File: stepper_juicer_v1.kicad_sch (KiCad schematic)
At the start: 12 parts, among them J1 Conn_01x06_Pin, J2 Barrel_Jack_Switch

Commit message: Schematic done
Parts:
- added C1, C11, C12, C14, C15, C6, C8, C9: 1uF 50V, Capacitor_SMD:C_0402_1005Metric, symbol Device:C
- added C10, C13, C3, C4, C7: 10uF 50V, Capacitor_SMD:C_0805_2012Metric, symbol Device:C
- added C2: 470uF 50V, Capacitor_THT:CP_Radial_D10.0mm_P5.00mm, symbol Device:C_Polarized_US
- added C5: 1uF 100V, Capacitor_SMD:C_0805_2012Metric, symbol Device:C
- added D1, D2, D3, D4: 30V 200mA, Diode_SMD:D_SOD-523, symbol Device:D_Schottky
- added D5, D6, D7, D8: 100V 2A, Diode_SMD:Nexperia_CFP3_SOD-123W, symbol Device:D_Schottky
- added D9: LED, Diode_SMD:D_0603_1608Metric, symbol Device:LED
- added J3: Conn_01x04_Pin, Connector_JST:JST_XH_B4B-XH-A_1x04_P2.50mm_Vertical, symbol Connector:Conn_01x04_Pin
- added J4: Conn_01x06_Pin, Connector_JST:JST_PH_B6B-PH-K_1x06_P2.00mm_Vertical, symbol Connector:Conn_01x06_Pin
- added Q1, Q2, Q3, Q4, Q5, Q6, Q7, Q8: NMOS, _custom_library: PG-TSDSON-8_3.8x2.29_Pitch0.65mm, symbol Simulation_SPICE:NMOS
- added R11, R13, R14, R16, R17, R19, R20: 4.7R, Resistor_SMD:R_0805_2012Metric, symbol Device:R_US
- added R12, R15, R18: 8.2R, Resistor_SMD:R_0805_2012Metric, symbol Device:R_US
- added R21: 8k2, Resistor_SMD:R_0603_1608Metric, symbol Device:R_US
- added U1, U2, U4, U5: NCP51513, Package_DFN_QFN:DFN-10-1EP_3x3mm_P0.5mm_EP1.7x2.5mm, symbol _custom_library:NCP51513
- added U3: ZXTR2012Z, Package_TO_SOT_SMD:SOT-89-3, symbol _custom_library:ZXTR2012Z
- J1: footprint (none) -> Connector_JST:JST_PH_B6B-PH-K_1x06_P2.00mm_Vertical; Link (none) -> https://www.digikey.ca/en/products/detail/jst-sales-america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
- J2: footprint (none) -> Connector_BarrelJack:BarrelJack_GCT_DCJ200-10-A_Horizontal; Link (none) -> https://www.digikey.ca/en/products/detail/tensility-interna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
- R1, R2: value 1k5 -> 2k0; footprint (none) -> Resistor_SMD:R_0603_1608Metric; Link (none) -> https://www.digikey.ca/en/products/detail/stackpole-electro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
- R10: value 1k5 -> 4.7R; footprint (none) -> Resistor_SMD:R_0805_2012Metric; Link (none) -> https://www.digikey.ca/en/products/detail/panasonic-electro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
- R3, R4, R5, R7, R8: footprint (none) -> Resistor_SMD:R_0603_1608Metric; Link (none) -> https://www.digikey.ca/en/products/detail/stackpole-electro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
- R6: value 1k5 -> 1k0; footprint (none) -> Resistor_SMD:R_0603_1608Metric; Link (none) -> https://www.digikey.ca/en/products/detail/stackpole-electro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
- R9: value 1k0 -> 8.2R; footprint (none) -> Resistor_SMD:R_0805_2012Metric; Link (none) -> https://www.digikey.ca/en/products/detail/panasonic-electro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
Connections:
- net +12V: now also C1.1, C10.1, C11.1, C13.1, C14.1, C3.1, C4.1, C7.1, C8.1, D5.2 (A), D6.2 (A), D7.2 (A), D8.2 (A), D9.2 (A), U1.1 (VCC), U1.6 (EN), U2.1 (VCC), U2.6 (EN), U3.3 (VOUT), U4.1 (VCC), U4.6 (EN), U5.1 (VCC), U5.6 (EN)
- net +48V: now also J2.1, C2.1, C5.1, Q1.1 (D), Q3.1 (D), Q5.1 (D), Q7.1 (D), U3.2 (VIN)
- net GND: now also J2.2, R6.2, R7.1, C1.2, C10.2, C11.2, C13.2, C14.2, C2.2, C3.2, C4.2, C5.2, C7.2, C8.2, D1.2 (A), D2.2 (A), D3.2 (A), D4.2 (A), Q2.3 (S), Q4.3 (S), Q6.3 (S), Q8.3 (S), R21.2, U1.11 (EP), U1.9 (GND), U2.11 (EP), U2.9 (GND), U3.1 (GND), U4.11 (EP), U4.9 (GND), U5.11 (EP), U5.9 (GND); no longer R7.2, R9.1
- net A_IN+: now reaches R1.1, R4.1
- net A_IN+: now also D1.1 (K), J3.1 (Pin_1), U1.8 (LIN), U4.7 (HIN); no longer R3.1
- net A_IN-: now reaches R2.1, R5.2
- net A_IN-: now also D2.1 (K), J3.2 (Pin_2), U1.7 (HIN), U4.8 (LIN); no longer R3.2
- net A+ renamed A_DRIVE+
- net A- renamed A_DRIVE-
- net B+ renamed B_DRIVE+
- net B_DRIVE+: now also R3.2; no longer R6.2
- net B-: no longer names the net of R10.2
- net B-: now also U1.10 (DRVL); no longer J1.6 (Pin_6)
- new net: Q3.2 (G), R13.1
- new net: R13.2, U2.4 (DRVH)
- new net: C6.1, R9.1, U1.3 (VB)
- new net: R11.2, U1.4 (DRVH)
- new net: D9.1 (K), R21.1
- new net: C12.1, R15.1, U4.3 (VB)
- new net: C9.1, R12.1, U2.3 (VB)
- new net: D6.1 (K), R12.2
- new net: R20.2, U5.10 (DRVL)
- new net: C15.1, R18.1, U5.3 (VB)
- new net: R19.2, U5.4 (DRVH)
- new net: R14.2, U2.10 (DRVL)
- new net: R17.2, U4.10 (DRVL)
- new net: R16.2, U4.4 (DRVH)
- new net: D7.1 (K), R15.2
- new net: Q6.2 (G), R17.1
- new net: Q1.2 (G), R11.1
- new net: Q5.2 (G), R16.1
- new net: Q7.2 (G), R19.1
- new net: Q4.2 (G), R14.1
- new net: Q8.2 (G), R20.1
- new net: D5.1 (K), R9.2
- new net: D8.1 (K), R18.2
- new net: Q2.2 (G), R10.1
- new net A_OUT+: C12.2, J4.1 (Pin_1), Q5.3 (S), Q6.1 (D), U4.5 (HB)
- new net A_OUT-: C6.2, J4.3 (Pin_3), Q1.3 (S), Q2.1 (D), U1.5 (HB)
- new net B_DRIVE-: J1.6 (Pin_6), R8.2
- new net B_IN+: D3.1 (K), J3.3 (Pin_3), R3.1, R6.1, U2.7 (HIN), U5.8 (LIN)
- new net B_IN-: D4.1 (K), J3.4 (Pin_4), R7.2, R8.1, U2.8 (LIN), U5.7 (HIN)
- new net B_OUT+: C9.2, J4.4 (Pin_4), Q3.3 (S), Q4.1 (D), U2.5 (HB)
- new net B_OUT-: C15.2, J4.6 (Pin_6), Q7.3 (S), Q8.1 (D), U5.5 (HB)
- no-connect marks 0 -> 5
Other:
- note added: "Assuming the stepper is driven by 24V, this attenuation should give us -0.3 to 4.5V at the gate driver inputs. The driver can take an absolute minimum of -5V. The logid low threshold is 0.8V, nd the high threshold is 2.3V. Current draw from the previous driver is 4.8mV. The input pull down is 175k, which should only have an insignificant effect on the input voltages."
- note added: "H-BRIDGES AND OUTPUT"
- note added: "INPUT"
- note added: "POWER"
- note added: "Populating this connector and unpoplating the entire resistor divider chunk allows us to drive a 2-phase stepper with custom PWM signals instead."
- note added: "The following is assuming a 10kHz PWM with worst case scenario duty cycle 80% and charging 10%: Required bootstrap capacitance = (80us*100uA + 9.1nC) / (12V * 1%) = 143nF. I want to be on the safe side, so choose 1uF. Then, the bootstrap resistance = 10us / (1uF * ln((11.17-11.05)/(11.17-11.12))) = 11.4R Schottky diode drop is 0.83V, giving 12 - 0.83 = 11.17V. We're also taking the final capacito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"
- note removed: "Assuming the stepper is driven by 24V, this 1/4 attenuation should give us -3 to 3V at the gate driver inputs. The driver can take an absolute minimum of -5V. The low threshold is 0.8V, nd the high threshold is 2.3V. The input pull down is 175k, which should only have an insignificant effect on the input voltages."
- moved on the sheet: J1, J2, R1, R2, R4, R5

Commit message: Finish design
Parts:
- removed C1, C11, C14, C8: 1uF 50V, Capacitor_SMD:C_0402_1005Metric, symbol Device:C
- added H1, H2, H3: M3 Pad, MountingHole:MountingHole_3.2mm_M3_Pad, symbol Mechanical:MountingHole_Pad
- added TP1, TP2, TP3: TestPoint, TestPoint:TestPoint_Pad_D1.0mm, symbol Connector:TestPoint
- C12, C15, C6, C9: footprint Capacitor_SMD:C_0402_1005Metric -> Capacitor_SMD:C_0805_2012Metric; Link https://www.digikey.ca/en/products/detail/murata-electronics/GRM155R61H105KE05D/13531808 -> https://www.digikey.ca/en/products/detail/murata-electronics/GRJ21BC72A105KE11L/5321010
- D5, D6, D7, D8: value 100V 2A -> 100V 200mA; footprint Diode_SMD:Nexperia_CFP3_SOD-123W -> Diode_SMD:D_SOD-323F; Link https://www.digikey.ca/en/products/detail/nexperia-usa-inc/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 -> https://www.digikey.ca/en/products/detail/onsemi/NSR02100HT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
- R12, R15, R18, R9: footprint Resistor_SMD:R_0805_2012Metric -> Resistor_SMD:R_0603_1608Metric; Link https://www.digikey.ca/en/products/detail/panasonic-electronic-components/ERJ-P06J7R5V/9812041 -> https://www.digikey.ca/en/products/detail/panasonic-electronic-components/ERJ-3BQF8R2V/5647424
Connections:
- net +12V: now also TP2.1
- net +48V: now also TP1.1
- net GND: now also TP3.1
- no-connect marks 5 -> 8
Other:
- moved on the sheet: C10, C13, C3, C7

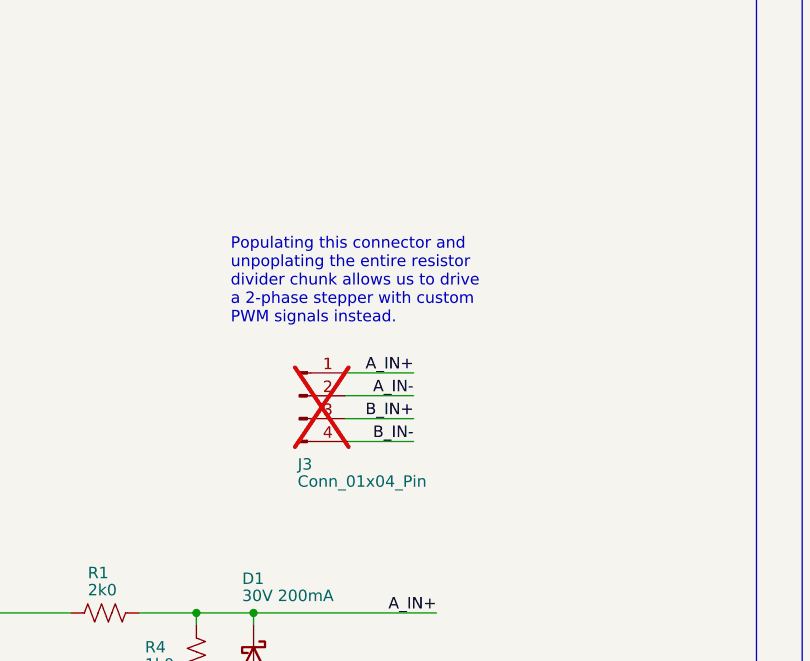
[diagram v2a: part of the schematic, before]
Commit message: Add ground pin
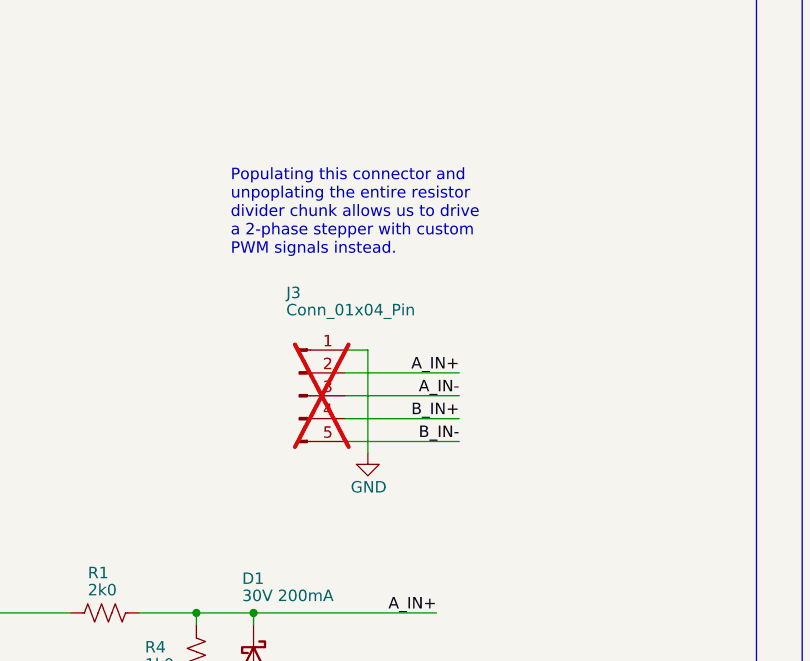
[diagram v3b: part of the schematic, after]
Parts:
- J3: footprint Connector_JST:JST_XH_B4B-XH-A_1x04_P2.50mm_Vertical -> Connector_JST:JST_XH_B5B-XH-A_1x05_P2.50mm_Vertical; symbol Connector:Conn_01x04_Pin -> Connector:Conn_01x05_Pin
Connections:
- net A_IN+: now also J3.2 (Pin_2); no longer J3.1 (Pin_1)
- net A_IN-: now also J3.3 (Pin_3); no longer J3.2 (Pin_2)
- net B_IN+: now also J3.4 (Pin_4); no longer J3.3 (Pin_3)
- net B_IN-: now also J3.5 (Pin_5); no longer J3.4 (Pin_4)
- net GND: now also J3.1 (Pin_1)
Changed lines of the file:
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@@
 	(text "Populating this connector and \nunpoplating the entire resistor\ndivider chunk allows us to drive \na 2-phase stepper with custom\nPWM signals instead."
 		(exclude_from_sim no)
-		(at 83.82 95.25 0)
+		(at 83.82 87.63 0)
 		(effects
 			(font
@@
 	(wire
 		(pts
-			(xy 104.14 107.95) (xy 96.52 107.95)
-		)
-		(stroke
-			(width 0)
-			(type default)
-		)
-	)
-	(wire
-		(pts
 			(xy 228.6 147.32) (xy 223.52 147.32)
 		)
@@
 	(wire
 		(pts
+			(xy 96.52 110.49) (xy 109.22 110.49)
+		)
+		(stroke
+			(width 0)
+			(type default)
+		)
+	)
+	(wire
+		(pts
 			(xy 198.12 265.43) (xy 200.66 265.43)
 		)
@@
 	(wire
 		(pts
+			(xy 96.52 105.41) (xy 109.22 105.41)
+		)
+		(stroke
+			(width 0)
+			(type default)
+		)
+	)
+	(wire
+		(pts
 			(xy 190.5 190.5) (xy 189.23 190.5)
 		)
@@
 	(wire
 		(pts
-			(xy 104.14 113.03) (xy 96.52 113.03)
-		)
-		(stroke
-			(width 0)
-			(type default)
-		)
-	)
-	(wire
-		(pts
 			(xy 57.15 36.83) (xy 60.96 36.83)
 		)
@@
 	(wire
 		(pts
+			(xy 99.06 102.87) (xy 99.06 114.3)
+		)
+		(stroke
+			(width 0)
+			(type default)
+		)
+	)
+	(wire
+		(pts
 			(xy 264.16 36.83) (xy 264.16 39.37)
 		)
@@
 	(wire
 		(pts
+			(xy 96.52 107.95) (xy 109.22 107.95)
+		)
+		(stroke
+			(width 0)
+			(type default)
+		)
+	)
+	(wire
+		(pts
 			(xy 95.25 142.24) (xy 95.25 144.78)
 		)
@@
 	(wire
 		(pts
-			(xy 104.14 105.41) (xy 96.52 105.41)
+			(xy 99.06 102.87) (xy 96.52 102.87)
 		)
 		(stroke
@@
 	(wire
 		(pts
+			(xy 96.52 113.03) (xy 109.22 113.03)
+		)
+		(stroke
+			(width 0)
+			(type default)
+		)
+	)
+	(wire
+		(pts
 			(xy 246.38 88.9) (xy 246.38 90.17)
 		)
@@
 	(wire
 		(pts
-			(xy 104.14 110.49) (xy 96.52 110.49)
-		)
-		(stroke
-			(width 0)
-			(type default)
-		)
-	)
-	(wire
-		(pts
 			(xy 80.01 187.96) (xy 80.01 186.69)
 		)
@@
 	)
 	(label "B_IN+"
-		(at 104.14 110.49 180)
+		(at 109.22 110.49 180)
 		(effects
 			(font
@@
 	)
 	(label "B_IN-"
-		(at 104.14 113.03 180)
+		(at 109.22 113.03 180)
 		(effects
 			(font
@@
 	)
 	(label "A_IN-"
-		(at 104.14 107.95 180)
+		(at 109.22 107.95 180)
 		(effects
 			(font
@@
 	)
 	(label "A_IN+"
-		(at 104.14 105.41 180)
+		(at 109.22 105.41 180)
 		(effects
 			(font
@@
 	)
 	(symbol
-		(lib_id "Connector:Conn_01x04_Pin")
+		(lib_id "Connector:Conn_01x05_Pin")
 		(at 91.44 107.95 0)
 		(unit 1)
@@
 		(dnp yes)
 		(property "Reference" "J3"
-			(at 92.075 115.57 0)
+			(at 90.805 96.52 0)
 			(effects
 				(font
@@
 		)
 		(property "Value" "Conn_01x04_Pin"
-			(at 98.425 117.475 0)
+			(at 97.155 98.425 0)
 			(effects
 				(font
@@
 			)
 		)
-		(property "Footprint" "Connector_JST:JST_XH_B4B-XH-A_1x04_P2.50mm_Vertical"
+		(property "Footprint" "Connector_JST:JST_XH_B5B-XH-A_1x05_P2.50mm_Vertical"
 			(at 91.44 107.95 0)
 			(effects
@@
 			)
 		)
-		(property "Description" "Generic connector, single row, 01x04, script generated"
+		(property "Description" "Generic connector, single row, 01x05, script generated"
 			(at 91.44 107.95 0)
 			(effects
@@
 		(pin "1"
 		)
+		(pin "5"
+		)
 		(instances
 			(project ""
@@
 					(unit 1)
 				)
+			)
+		)
+	)
+	(symbol
+		(lib_id "power:GND")
+		(at 99.06 114.3 0)
+		(unit 1)
+		(exclude_from_sim no)
+		(in_bom yes)
+		(on_board yes)
+		(dnp no)
+		(property "Reference" "#PWR035"
+			(at 99.06 120.65 0)
+			(effects
+				(font
+					(size 1.27 1.27)
+				)
+				(justify left)
+				(hide yes)
+			)
+		)
+		(property "Value" "GND"
+			(at 97.155 118.11 0)
+			(effects
+				(font
+					(size 1.27 1.27)
+				)
+				(justify left)
+			)
+		)
+		(property "Footprint" ""
+			(at 99.06 114.3 0)
+			(effects
+				(font
+					(size 1.27 1.27)
+				)
+				(justify left)
+				(hide yes)
+			)
+		)
+		(property "Datasheet" ""
+			(at 99.06 114.3 0)
+			(effects
+				(font
+					(size 1.27 1.27)
+				)
+				(justify left)
+				(hide yes)
+			)
+		)
+		(property "Description" "Power symbol creates a global label with name \"GND\" , ground"
+			(at 99.06 114.3 0)
+			(effects
+				(font
+					(size 1.27 1.27)
+				)
+				(justify left)
+				(hide yes)
+			)
+		)
+		(pin "1"
+		)
+		(instances
+			(project "stepper_juicer_v1"
+				(path "/21223b99-bae8-49fe-9057-f65e2fd7129d"
+					(reference "#PWR035")
+					(unit 1)
+				)
